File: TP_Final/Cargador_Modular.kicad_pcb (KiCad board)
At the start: 2 copper layers, 198.1 x 99.7 mm, 183 parts, among them J101 BG 1x2, J102 BG 1x2, J103 BG 1x2, J104 BG 1x3, J105 Pin Header1x4, J106 Pin socket 2x4, J107 Pin Header 2x3, J108 BG2, J109 2 x BG2, J110 BG2, J111 Conector pol. 1x3, J112 BG2, J113 Conector pol. 1x3, J114 Conector pol. 1x3, J115 BG2, J116 BG2, K101 2FORM-C 2A 12VCC, K102 2FORM-C 2A 12VCC, K103 2FORM-C 2A 12VCC, K104 2FORM-C 2A 12VCC, Q101 2N3904, Q102 2N3904, Q103 2N3904, Q104 2N3904, Q105 2N3904, Q106 2N3904, Q107 2N3904, Q108 2N3904, Q109 2N3904, Q110 2N3904, SW101 SW_Push, SW102 KS01-B, SW103 KS01-B, SW104 KS01-B, SW105 KS01-B, U101 LM35-ZD, U102 STM32F103RBTx, U103 24LC256, U104 OP07, U105 OP07, U106 OP07, U107 LM7805_TO220, U108 LD1117S33TR_SOT223, Y101 8Mhz, Y102 32.768Khz

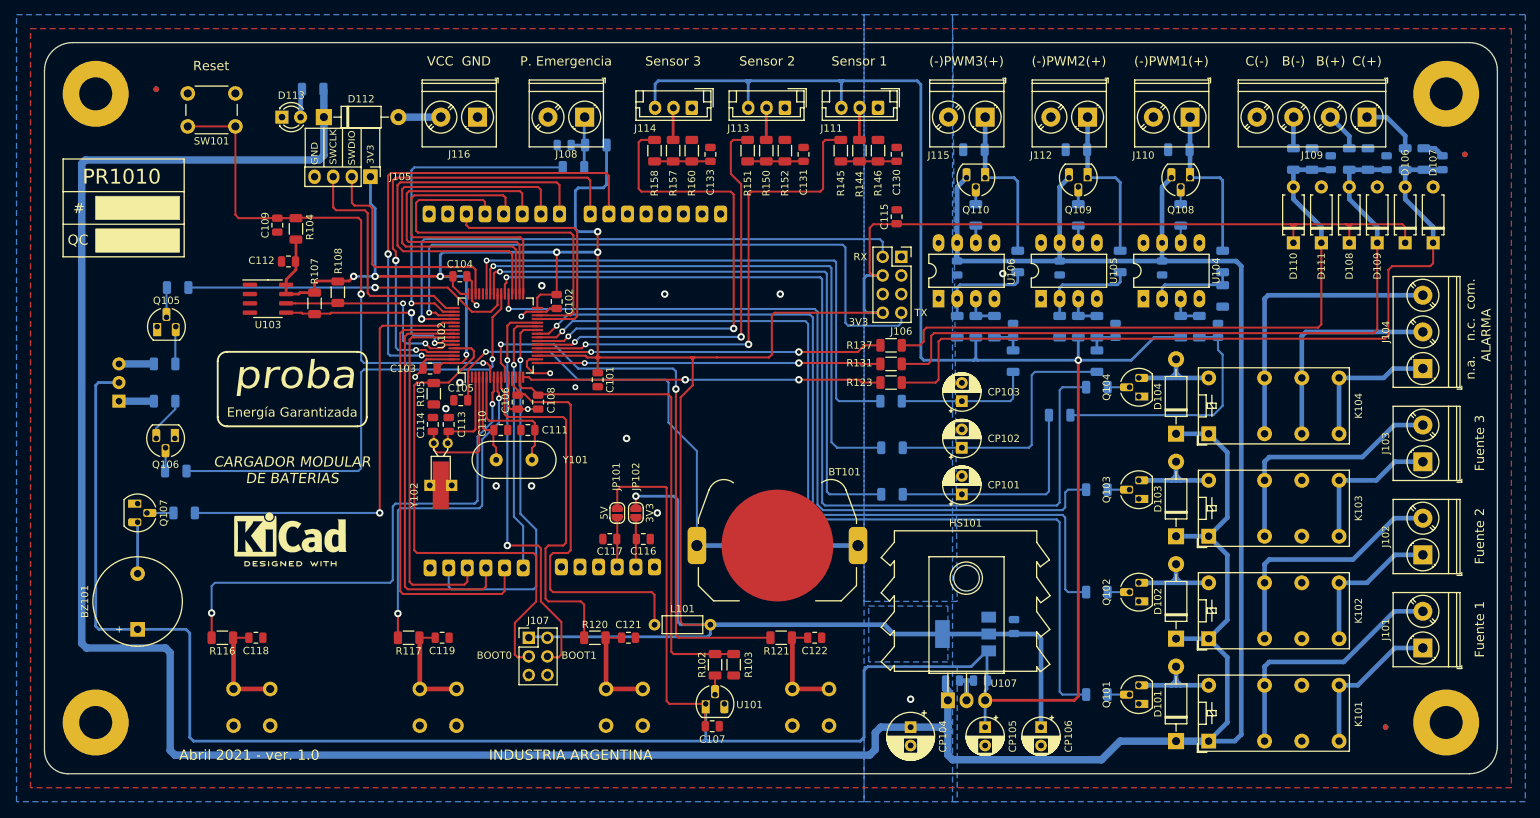
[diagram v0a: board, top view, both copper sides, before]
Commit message: Correccion bordes, fabricante y licencia
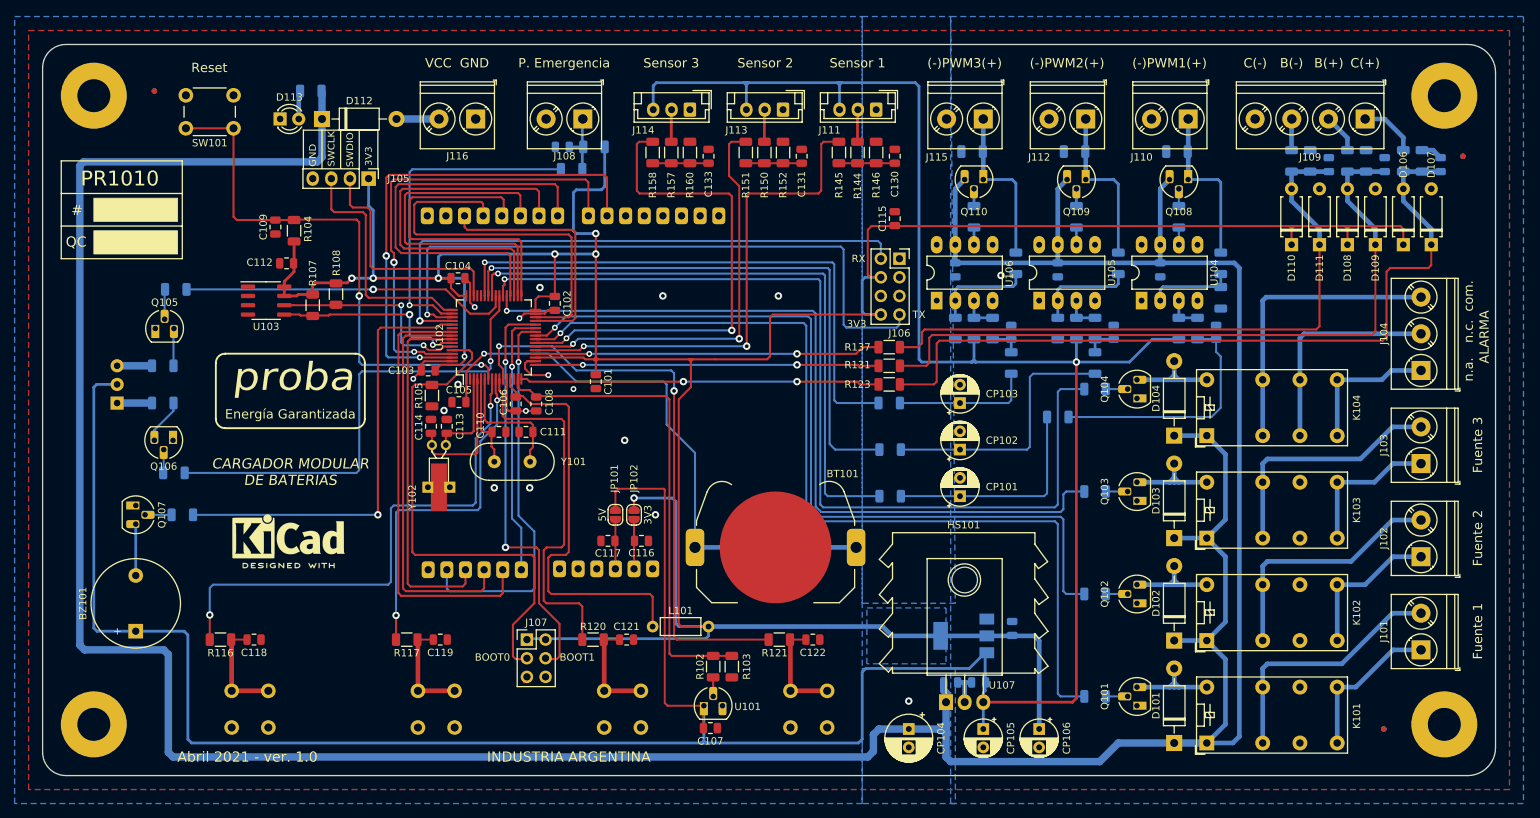
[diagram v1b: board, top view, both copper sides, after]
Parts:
- moved C107 0.36 mm to (127.9, 135.8)
- moved D102 0.36 mm to (191.1, 123.8)
- moved D103 0.36 mm to (191.1, 109.9)
- moved D104 0.36 mm to (191.1, 95.9)
- moved J101 0.36 mm to (224.8, 125.1)
- moved J104 0.36 mm to (224.8, 87.0)
- moved J113 0.36 mm to (137.8, 51.4)
- moved R127 0.36 mm to (175.3, 93.3)
- moved R138 0.36 mm to (209.7, 58.4)
- moved R147 0.36 mm to (183.5, 72.4)
- moved R148 0.36 mm to (175.3, 81.3)
- moved R161 0.36 mm to (169.5, 72.4)
- moved R162 0.36 mm to (161.3, 81.3)
- moved C124 0.36 mm to (227.5, 58.9)
- moved C126 0.36 mm to (219.8, 58.9)
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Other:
- outline, holes or cut-outs redrawn
- board text added: "Estandares de fabricaión según Mayer: Terminación superficial : HASL Espesor final aprox. :1.6mm Material: FR4 Grillas usadas: 25mils, 5mils, 0.5mils Trazos usados: 40mils, 25mils, 15mils y 11mils Vías usadas: 31.5/15.7 mils y 40/20mils Separación mínima entre trazas: 7mils / 0.18mm Distancia de cobre a borde mayor a: 40mils / 1mm"
- board text removed: "Terminación superficial : HASL Espesor final aprox. :1.6mm Material: FR4 Grillas usadas: 25mils, 5mils, 0.5mils Trazos usados: 40mils, 25mils, 15mils y 11mils Vías usadas: 31.5/15.7 mils y 40/20mils Separación mínima entre trazas: 7mils / 0.18mm Distancia de cobre a borde: 20mils / 0.5mm"
